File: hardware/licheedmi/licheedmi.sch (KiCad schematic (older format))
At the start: 74 parts, among them J1 Conn_01x09, J2 HDMI_A_PCB, J3 LicheePiNano_LCD, J4 HDMI_A, J5 USB_C_Receptacle_USB2.0, U1 SiI9022A, U2 LicheeNano, U3 TS3DV20812, U4 TLV74312PDBVR, U5 CH340C

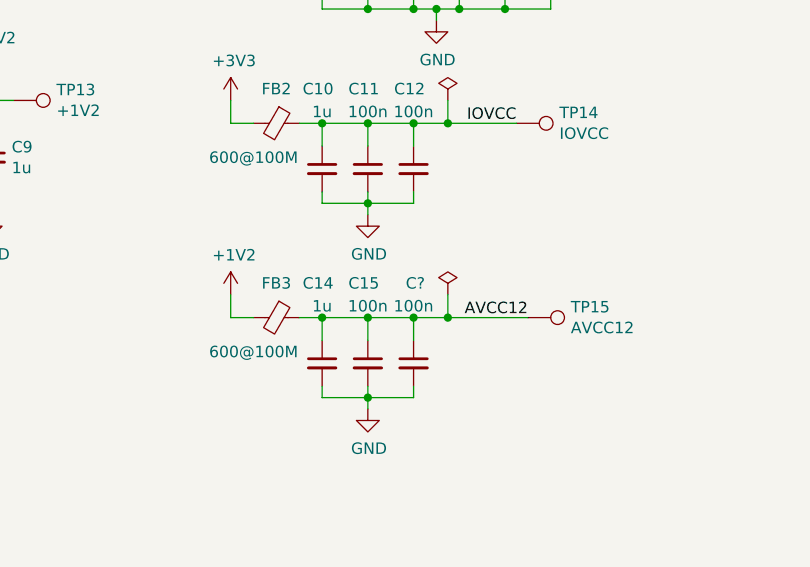
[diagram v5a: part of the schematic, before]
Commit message: sch: Add missing C17 cap
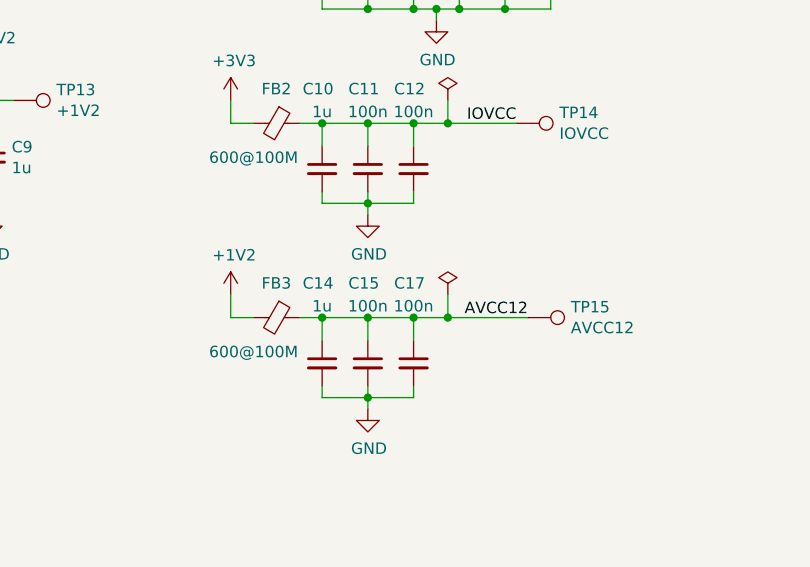
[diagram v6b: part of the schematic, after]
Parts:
- gave numbers to parts that had none: 1
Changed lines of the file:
@@
 $EndComp
 $Comp
-L Device:C_Small C?
+L Device:C_Small C17
 U 1 1 5FD5762A
 P 4600 9950
-F 0 "C?" H 4650 10300 50  0000 R CNN
+F 0 "C17" H 4650 10300 50  0000 R CNN
 F 1 "100n" H 4600 10200 50  0000 C CNN
 F 2 "Capacitor_SMD:C_0603_1608Metric" H 4600 9950 50  0001 C CNN
